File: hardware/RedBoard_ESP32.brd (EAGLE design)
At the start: 68.6 x 58.4 mm, 110 parts, among them J1 5.5x2.1mm Barrel, J13 QWIIC_RIGHT_ANGLE, J15 MICRO-SDPUSH-PUSH, J2 USB C, J3 USB_SOLDER_PADS, J5 M10NO_SILK, Q1 MBT3904DW1T1, Q11 20V/4.2A/52mΩ/1.4W, Q13 20V/4.2A/52mΩ/1.4W, Q3 20V/4.2A/52mΩ/1.4W, Q5 20V/4.2A/52mΩ/1.4W, Q7 20V/4.2A/52mΩ/1.4W, Q9 20V/4.2A/52mΩ/1.4W, U1 ESP-WROOM-3232D-NARROW, U2 CH340C, U3 LM1117, U4 3.3V, U5 MCP73831, U6 MAX17048

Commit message: Added missing Vin symbol.
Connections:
- removed net N$9: C9.+, D1.C, U3.3
- net VIN: now also C9.+, D1.C, U3.3
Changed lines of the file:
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@@
 <contactref element="J9" pad="8"/>
 <contactref element="J10" pad="8"/>
-<wire x1="45.72" y1="1.27" x2="45.72" y2="6.732" width="0" layer="19" extent="1-1"/>
+<contactref element="C9" pad="+"/>
+<contactref element="D1" pad="C"/>
+<contactref element="U3" pad="3"/>
+<wire x1="-63.64" y1="-764.54" x2="-71.3486" y2="-768.9088" width="0" layer="19" extent="1-1"/>
+<wire x1="-56.27" y1="-763.27" x2="-63.64" y2="-764.54" width="0" layer="19" extent="1-1"/>
+<wire x1="45.72" y1="1.27" x2="-56.27" y2="-763.27" width="0" layer="19" extent="1-1"/>
+<wire x1="45.72" y1="6.732" x2="45.72" y2="1.27" width="0" layer="19" extent="1-1"/>
 </signal>
 <signal name="VUSB" class="1">
@@
 <wire x1="-61.81" y1="-772.16" x2="-63.92" y2="-772.16" width="0" layer="19" extent="1-1"/>
 </signal>
-<signal name="N$9" class="1">
-<contactref element="C9" pad="+"/>
-<contactref element="D1" pad="C"/>
-<contactref element="U3" pad="3"/>
-<wire x1="-63.64" y1="-764.54" x2="-71.3486" y2="-768.9088" width="0" layer="19" extent="1-1"/>
-<wire x1="-56.27" y1="-763.27" x2="-63.64" y2="-764.54" width="0" layer="19" extent="1-1"/>
-</signal>
 <signal name="N$12">

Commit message: Changed pin name from /SS to /CS
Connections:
- net ESP32_GPIO5_!SS! renamed ESP32_GPIO5_!CS!
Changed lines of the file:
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@@
 <wire x1="0" y1="-547.37" x2="45.8" y2="15.892" width="0" layer="19" extent="1-1"/>
 </signal>
-<signal name="ESP32_GPIO5_!SS!">
+<signal name="ESP32_GPIO5_!CS!">
 <contactref element="U1" pad="29"/>
 <contactref element="J15" pad="CS/DAT3"/>

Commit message: Preliminary routed board, no labels yet.
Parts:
- LOGO1: value SFE_LOGO_NAME_FLAME6_MM -> SFE_LOGO_NAME.1_INCH; device SparkFun-Aesthetics:SFE_LOGO_NAME_FLAME_6MM -> SparkFun-Aesthetics:SFE_LOGO_NAME_.1
- moved LOGO4 973.6 mm to (10.2, 56.9), flipped to the bottom
- moved LOGO2 962.8 mm to (10.2, 51.1)
- moved R8 945.3 mm to (26.7, 38.1)
- moved D5 942.0 mm to (31.8, 38.1), turned to 180 degrees
- moved J14 939.5 mm to (19.7, 40.6), turned to 90 degrees
- moved JP10 935.5 mm to (22.2, 41.9), flipped to the bottom, turned to 90 degrees
- moved LOGO1 926.1 mm to (48.8, 12.4)
- moved LOGO3 925.7 mm to (9.91, 11.2), flipped to the bottom
- moved C17 899.9 mm to (21.6, 13.3)
- moved R25 897.9 mm to (36.8, 18.4), turned to 180 degrees
- moved Q10 895.5 mm to (33.0, 20.3), turned to 270 degrees
- moved R26 895.5 mm to (36.8, 16.5), turned to 180 degrees
- moved R24 893.5 mm to (36.8, 20.3), turned to 180 degrees
- moved R27 893.2 mm to (36.8, 14.6), turned to 180 degrees
- moved U6 891.3 mm to (17.8, 10.2)
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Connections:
- removed net SHLD: J2.SHLD1, J2.SHLD2, J2.SHLD3, J2.SHLD4
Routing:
- net ESP32_SCL: track 0.00 -> 180.8 mm, vias 0 -> 7
- net ESP32_SDA: track 0.00 -> 164.2 mm, vias 0 -> 5
- net ESP32_GPIO19_CIPO: track 0.00 -> 145.0 mm, vias 0 -> 5
- net ESP32_RXD0: track 0.00 -> 121.2 mm, vias 0 -> 5
- net ESP32_GPIO23_COPI: track 0.00 -> 114.0 mm, vias 0 -> 3
- net 5V: track 0.00 -> 114.0 mm, vias 0 -> 1
- net ESP32_GPIO18_SCK: track 0.00 -> 113.5 mm, vias 0 -> 4
- net ESP32_TXD0: track 0.00 -> 109.4 mm, vias 0 -> 6
- net V_USB: track 0.00 -> 108.9 mm, vias 0 -> 6
- net ESP32_GPIO5_!CS!: track 0.00 -> 104.5 mm, vias 0 -> 3
- net !GAUGE_ALERT!: track 0.00 -> 99.5 mm, vias 0 -> 4
- net ESP32_EN: track 0.00 -> 86.5 mm, vias 0 -> 2
- net 5V_CHG: track 0.00 -> 72.0 mm, vias 0 -> 4
- net 5V_MEAS: track 0.00 -> 64.7 mm, vias 0 -> 6
- net ESP32_GPIO4: track 0.00 -> 59.2 mm, vias 0 -> 2
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- added copper zone on layer 15, net 3.3V
- added copper zone on layer 1, net 5V_EXT
- added copper zone on layer 1, net GND
- added copper zone on layer 16, net GND
- added copper zone on layer 2, net GND
- added copper zone on layer 1, net V_BATT

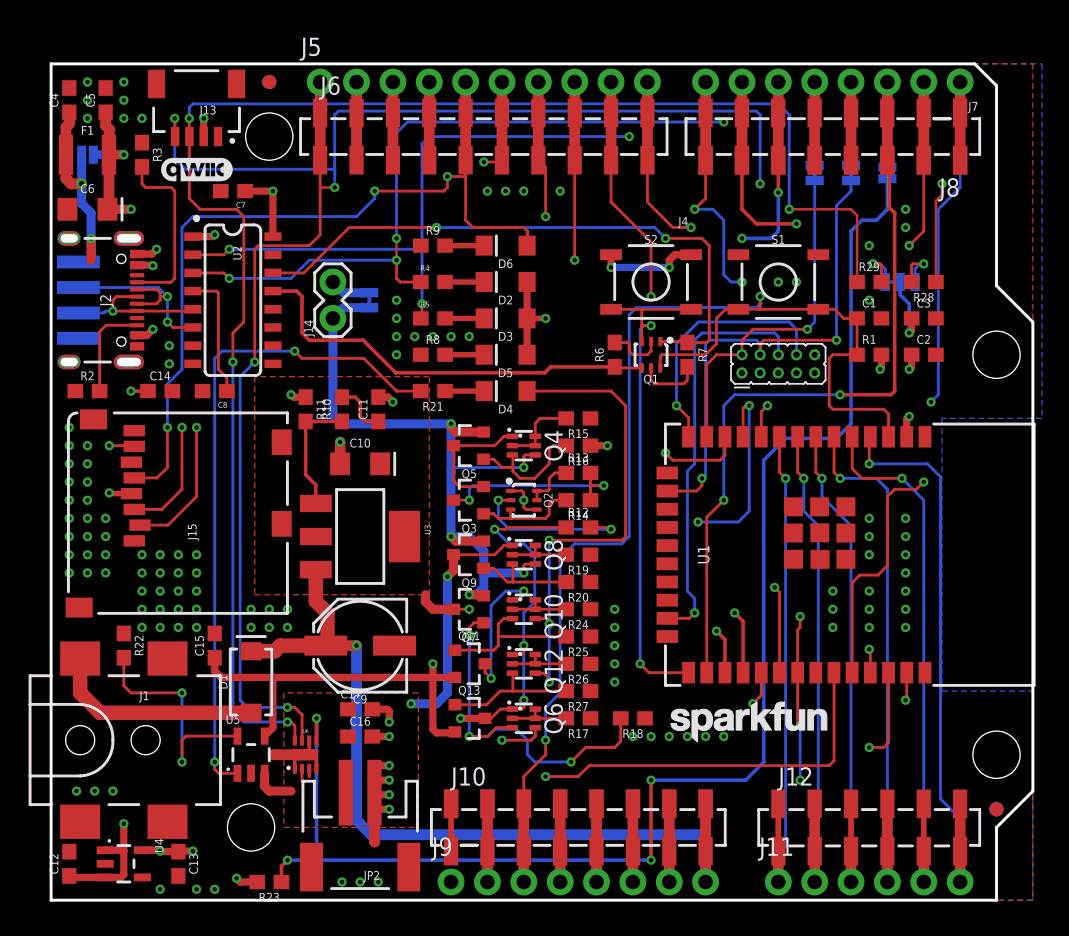
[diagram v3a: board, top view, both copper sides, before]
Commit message: Added board labels.
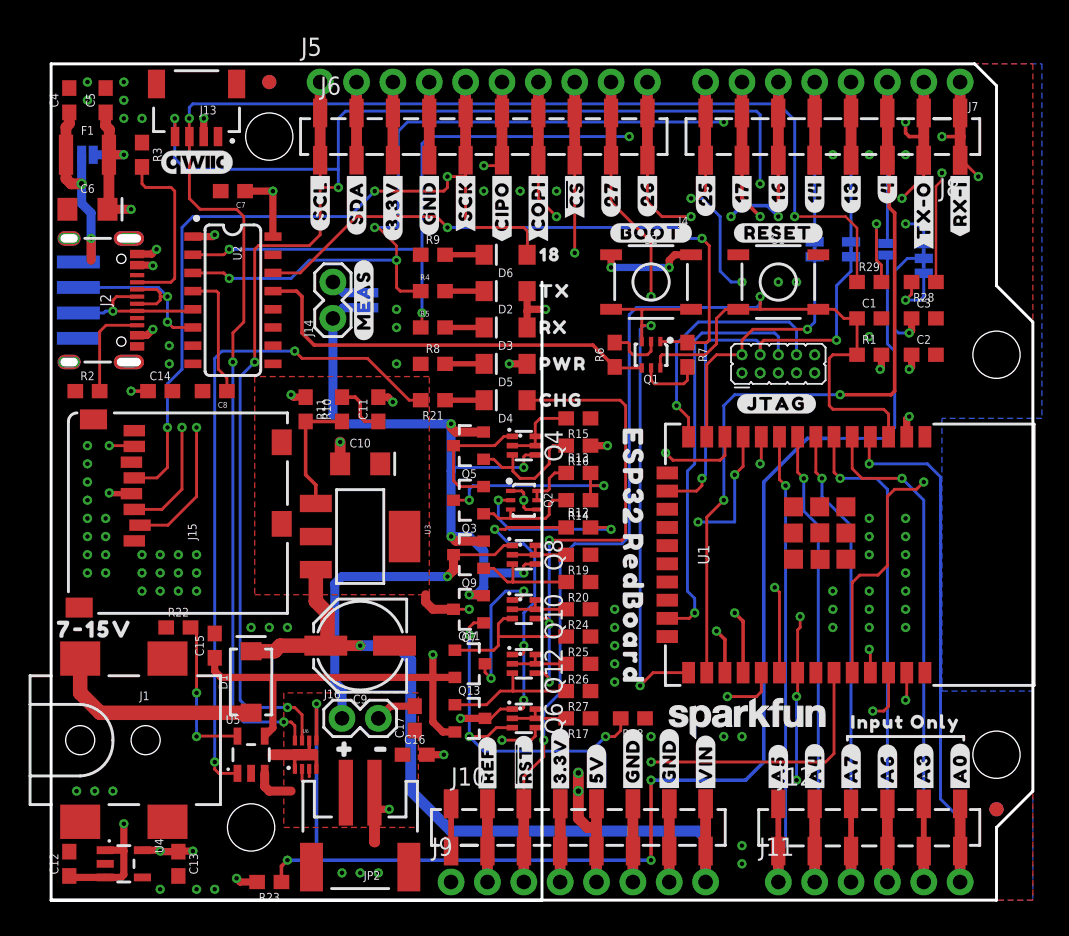
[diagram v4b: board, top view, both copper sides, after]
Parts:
- added J16: (no value), SparkFun-Connectors:1X02
- added LOGO5: SPECIAL_INSTRUCTIONS-ORDERING, SparkFun-Aesthetics:ORDERING_INSTRUCTIONS
- added LOGO6: SFE_LOGO_NAME_FLAME.2_INCH, SparkFun-Aesthetics:SFE_LOGO_NAME_FLAME_.2
- added U$10: (no value), output-ESP32:1836
- added U$11: (no value), output-ESP32:##CS##28
- added U$12: (no value), output-ESP32:#27#27
- added U$13: (no value), output-ESP32:#26#26
- added U$14: (no value), output-ESP32:TX1838
- added U$15: (no value), output-ESP32:RX1839
- added U$16: (no value), output-ESP32:PWR1837
- added U$17: (no value), output-ESP32:CHG1840
- added U$18: (no value), output-ESP32:#25#18
- added U$19: (no value), output-ESP32:#17#17
- added U$20: (no value), output-ESP32:#16#15
- added U$21: (no value), output-ESP32:#14#14
- added U$22: (no value), output-ESP32:#13#5
- added U$23: (no value), output-ESP32:#4#2
- added U$24: (no value), output-ESP32:#TX#O#0
- added U$25: (no value), output-ESP32:#RX#I#1
- added U$26: (no value), output-ESP32:#RESET#1842
- added U$27: (no value), output-ESP32:#BOOT#1841
- added U$28, U$46: (no value), output-ESP32:#JTAG#1847
- added U$29: (no value), output-ESP32:#A0#1843
- added U$3: (no value), output-ESP32:#SCL#34
- added U$30: (no value), output-ESP32:#A3#1843
- added U$31: (no value), output-ESP32:#A6#1843
- added U$32: (no value), output-ESP32:#A7#1843
- added U$33: (no value), output-ESP32:#A4#1843
- added U$34: (no value), output-ESP32:#A5#1843
- added U$35: (no value), output-ESP32:#VIN#1843
- added U$36, U$37: (no value), output-ESP32:#GND#1844
- added U$38: (no value), output-ESP32:#5V#1845
- added U$39: (no value), output-ESP32:#3#3V#1845
- added U$4: (no value), output-ESP32:#SDA#33
- added U$40: (no value), output-ESP32:##RST##1845
- added U$41: (no value), output-ESP32:#REF#1846
- added U$42, U$81: (no value), output-ESP32:#MEAS#1851
- added U$43, U$86: (no value), output-ESP32:#1849
- added U$44, U$88: (no value), output-ESP32:#1850
- added U$45: (no value), output-ESP32:#BATT#1848
- added U$47: (no value), output-ESP32:REDBOARD321856
- added U$48: (no value), output-ESP32:ESP321855
- added U$49: (no value), output-ESP32:7#15V32321861
- added U$5: (no value), output-ESP32:#3#3V#33
- added U$50: (no value), output-ESP32:#39#A3#32321865
- added U$51: (no value), output-ESP32:#36#A0#32321865
- added U$52: (no value), output-ESP32:#34#A6#32321865
- added U$53: (no value), output-ESP32:#35#A7#32321865
- added U$54: (no value), output-ESP32:#32#A4#32321865
- added U$55: (no value), output-ESP32:#33#A5#32321865
- added U$56: (no value), output-ESP32:#VIN#32321865
- added U$57, U$60: (no value), output-ESP32:#GND#32321866
- added U$58: (no value), output-ESP32:#5V#32321867
- added U$59: (no value), output-ESP32:#3#3V#32321867
- added U$6: (no value), output-ESP32:#GND#32
- added U$61: (no value), output-ESP32:##RST##32321867
- added U$62: (no value), output-ESP32:#IOREF#32321868
- added U$63: (no value), output-ESP32:#3#RX#I#32321869
- added U$64: (no value), output-ESP32:#1#TX#O#32321869
- added U$65: (no value), output-ESP32:#4#32321869
- added U$66: (no value), output-ESP32:#13#TCK#32321869
- added U$67: (no value), output-ESP32:#14#TMS#32321869
- added U$68: (no value), output-ESP32:#16#32321869
- added U$69: (no value), output-ESP32:#17#32321869
- added U$7: (no value), output-ESP32:#SCK#31
- added U$70: (no value), output-ESP32:#25#32321869
- added U$71: (no value), output-ESP32:#26#32321869
- added U$72: (no value), output-ESP32:#5##CS##32321869
- added U$73: (no value), output-ESP32:#23#COPI#32321869
- added U$74: (no value), output-ESP32:#19#CIPO#32321869
- added U$75: (no value), output-ESP32:#18#SCK#32321869
- added U$76: (no value), output-ESP32:#21#SDA#32321869
- added U$77: (no value), output-ESP32:#22#SCL#32321869
- added U$78: (no value), output-ESP32:#27#32321869
- added U$79: (no value), output-ESP32:#GND#32321869
- added U$8: (no value), output-ESP32:#CIPO#30
- added U$80: (no value), output-ESP32:#3#3V#32321869
- added U$82: (no value), output-ESP32:#BYP#35
- added U$83: (no value), output-ESP32:D#32321863
- added U$84: (no value), output-ESP32:D#32321862
- added U$85: (no value), output-ESP32:G32321864
- added U$89: (no value), output-ESP32:#I2C#1855
- added U$9: (no value), output-ESP32:#COPI#29
- added U$90: (no value), output-ESP32:##ALERT##1852
- added U$91: (no value), output-ESP32:#TMS#1854
- added U$92: (no value), output-ESP32:#TCK#1853
- added U$93: (no value), output-ESP32:ESP32_REDBOARD321857
- added U$94: (no value), output-ESP32:MADE_IN_THE_USA321857
- added U$96, U$97: (no value), output-ESP32:INPUT_ONLY321867
- moved FRAME1 79.2 mm to (5.59, 60.7)
- moved LOGO3 11.9 mm to (2.29, 2.03)
- moved JP12 5.33 mm to (58.4, 45.5)
- moved JP13 5.33 mm to (55.9, 45.5)
- moved JP14 5.33 mm to (53.3, 45.5)
- moved R22 4.02 mm to (8.89, 19.1), turned to 0 degrees
- moved C16 4.02 mm to (25.4, 10.2)
- moved C17 3.86 mm to (25.4, 12.7), turned to 90 degrees
- moved JP11 2.33 mm to (61.0, 44.8), turned to 270 degrees
- moved D4 0.64 mm to (31.8, 34.9)
- moved R21 0.64 mm to (26.7, 34.9)
- moved D2 0.63 mm to (31.8, 42.5)
- moved D3 0.63 mm to (31.8, 40.0)
- moved D5 0.63 mm to (31.8, 37.5)
- moved D6 0.63 mm to (31.8, 45.1)
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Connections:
- net GND: now also J16.2
- net V_BATT: now also J16.1
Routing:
- net V_BATT: track 21.3 -> 28.0 mm, vias 2 -> 1
- net ESP32_RXD0: track 121.2 -> 115.3 mm, vias 5 -> 6
- net N$14: track 16.6 -> 10.7 mm
- net ESP32_GPIO17: track 49.6 -> 44.0 mm
- net ESP32_GPIO4: track 59.2 -> 64.6 mm
- net ESP32_GPIO14_HDR: track 11.3 -> 16.6 mm
- net ESP32_GPIO13_HDR: track 11.3 -> 16.6 mm
- net ESP32_GPIO13_TCK: track 35.2 -> 29.8 mm
- net ESP32_GPIO14_TMS: track 24.3 -> 19.0 mm
- net N$20: track 3.74 -> 8.60 mm, vias 1 -> 2
- net ESP32_GPIO26: track 46.7 -> 42.6 mm
- net 5V: track 114.0 -> 110.6 mm, vias 1 -> 3
- net 3.3V: track 45.6 -> 48.1 mm, vias 12 -> 13
- net !GAUGE_ALERT!: track 99.5 -> 97.4 mm
- net ESP32_GPIO25: track 31.2 -> 33.3 mm
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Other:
- outline, holes or cut-outs redrawn
- board text added: "- Finish: HASL-Lead Free"

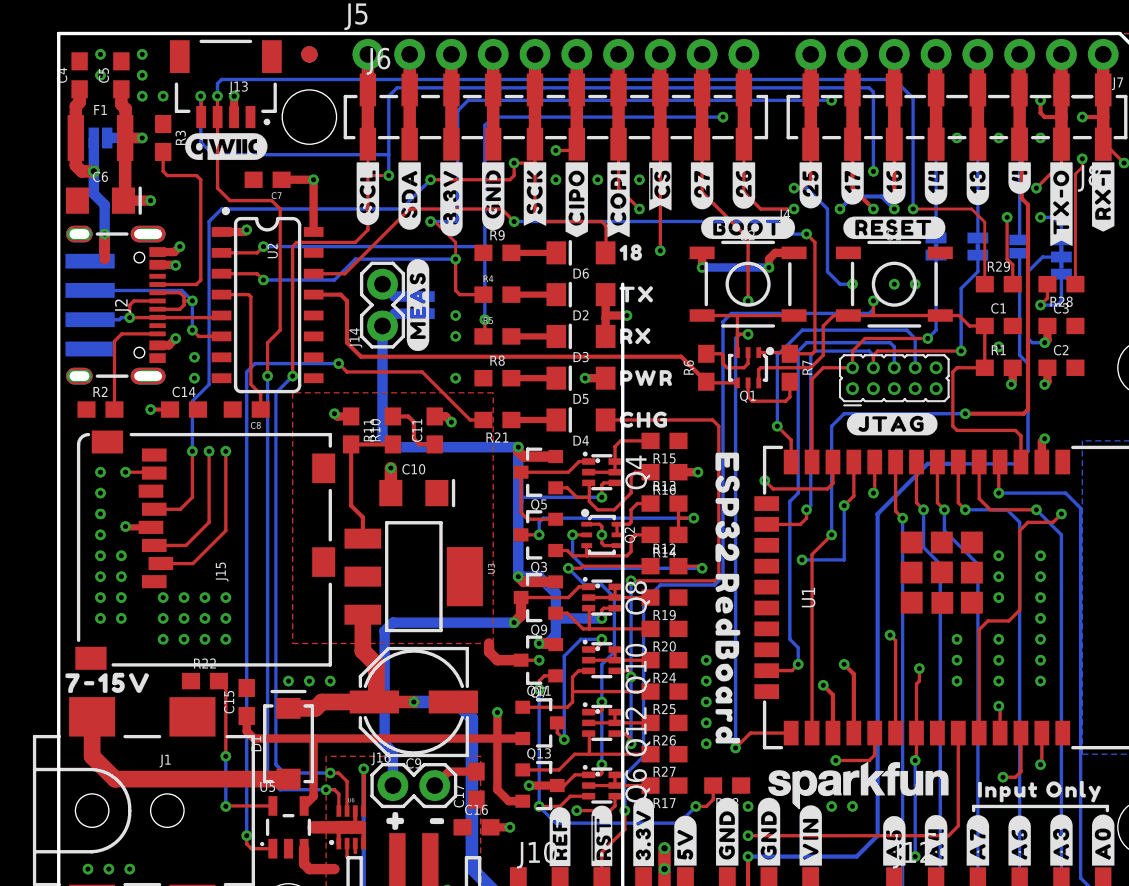
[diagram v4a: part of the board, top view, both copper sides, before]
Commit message: Added ordering instructions; added production files.
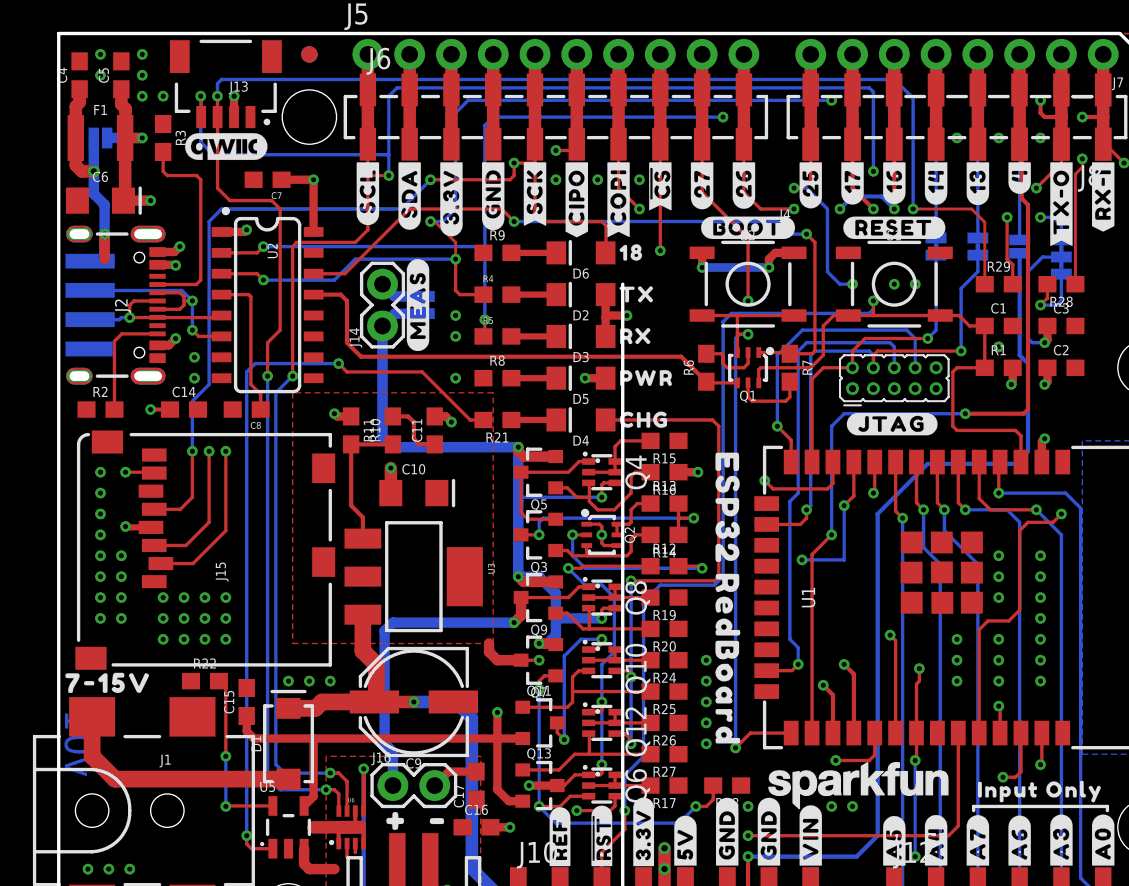
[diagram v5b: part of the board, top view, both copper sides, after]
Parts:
- U$65: device output-ESP32:#4#32321869 -> output-ESP32:##ALERT##4#321866
- moved U$65 0.13 mm to (58.4, 56.5)
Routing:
- net ESP32_TXD0: track 110.9 -> 110.2 mm
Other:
- board text added: "- 4 Layer Board"
- board text added: "- Board thickness is 1.6mm"
- board text added: "- No clean process"
- board text added: "v01"
- board text removed: "Units in inches"

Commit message: Changed board per Nathan's recommendations; added production files.
- Changed SPI pins nomenclatures.
- Fixed silkscreens.
- Replaced SD card socket with an updated one.
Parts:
- J14, J16: device SparkFun-Connectors:1X02 -> SparkFun-Connectors:1X02_NO_SILK
- J15: value MICRO-SDPUSH-PUSH -> MICRO-SD-PUSH-PUSH-EXT-PIN; device SparkFun-Connectors:MICRO-SD-SOCKET -> SparkFun-Connectors:MICROSD-EXTERNALPIN
- U$50: device output-ESP32:#39#A3#32321865 -> output-ESP32:#39#A3#321862
- U$51: device output-ESP32:#36#A0#32321865 -> output-ESP32:#36#A0#321862
- U$53: device output-ESP32:#35#A7#32321865 -> output-ESP32:#35#A7#321862
- U$55: device output-ESP32:#33#A5#32321865 -> output-ESP32:#34#A6#321862
- U$56: device output-ESP32:#VIN#32321865 -> output-ESP32:#VIN#321862
- U$57, U$60: device output-ESP32:#GND#32321866 -> output-ESP32:#GND#321863
- U$58: device output-ESP32:#5V#32321867 -> output-ESP32:#5V#321864
- U$59: device output-ESP32:#3#3V#32321867 -> output-ESP32:#3#3V#321864
- U$61: device output-ESP32:##RST##32321867 -> output-ESP32:##RESET##321864
- U$62: device output-ESP32:#IOREF#32321868 -> output-ESP32:#IOREF#321865
- U$73: device output-ESP32:#23#COPI#32321869 -> output-ESP32:#23#PICO#321866
- U$74: device output-ESP32:#19#CIPO#32321869 -> output-ESP32:#19#POCI#321866
- U$79: device output-ESP32:#GND#32321869 -> output-ESP32:#GND#321866
- U$8: device output-ESP32:#CIPO#30 -> output-ESP32:#POCI#30
- U$80: device output-ESP32:#3#3V#32321869 -> output-ESP32:#3#3V#321866
- U$9: device output-ESP32:#COPI#29 -> output-ESP32:#PICO#29
- moved LOGO1 36.8 mm to (15.4, 28.4), turned to 270 degrees
- moved R23 33.2 mm to (48.3, 5.08), turned to 270 degrees
- moved R22 18.9 mm to (15.2, 1.27), turned to 180 degrees
- moved C14 16.4 mm to (17.1, 48.9), turned to 90 degrees
- moved J15 16.0 mm to (2.03, 27.3), turned to 270 degrees
- moved C8 14.3 mm to (6.35, 48.9), turned to 90 degrees
- moved U$49 4.83 mm to (7.87, 19.1)
- moved R3 3.70 mm to (8.26, 48.9)
- moved R2 3.24 mm to (5.71, 36.2), turned to 180 degrees
- turned C11 to 270 degrees
- turned U$81 to 90 degrees
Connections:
- removed net ESP32_GPIO19_CIPO: J15.DO/DAT0, J5.6, J6.6A, J6.6B, U1.31
- removed net ESP32_GPIO23_COPI: J15.DI/CMD, J5.7, J6.7A, J6.7B, U1.37
- new net ESP32_GPIO19_POCI: J15.7, J5.6, J6.6A, J6.6B, U1.31
- new net ESP32_GPIO23_PICO: J15.3, J5.7, J6.7A, J6.7B, U1.37
- net 3.3V: now also J15.4; no longer J15.VCC
- net ESP32_GPIO18_SCK: now also J15.5; no longer J15.SCLK
- net ESP32_GPIO5_!CS!: now also J15.2; no longer J15.CS/DAT3
- net GND: now also J15.10, J15.11, J15.12, J15.13, J15.6; no longer J15.GND, J15.GND1, J15.GND3
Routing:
- net ESP32_GPIO19_POCI: track 0.00 -> 149.6 mm, vias 0 -> 5
- net ESP32_GPIO19_CIPO: track 143.9 -> 0.00 mm, vias 5 -> 0
- net ESP32_GPIO23_PICO: track 0.00 -> 114.5 mm, vias 0 -> 3
- net ESP32_GPIO23_COPI: track 114.3 -> 0.00 mm, vias 3 -> 0
- net V_USB: track 108.9 -> 115.9 mm, vias 6 -> 5
- net CC1: track 12.5 -> 6.75 mm
- net N$6: track 8.94 -> 14.4 mm, vias 0 -> 2
- net N$14: track 10.7 -> 15.0 mm, vias 2 -> 0
- net GND: track 49.2 -> 53.0 mm, vias 93 -> 83
- net ESP32_GPIO18_SCK: track 113.5 -> 115.9 mm
- net 3.3V: track 48.1 -> 50.4 mm, vias 13 -> 12
- net !GAUGE_ALERT!: track 97.4 -> 95.3 mm
- net 5V_EXT: track 39.5 -> 38.2 mm
- net ESP32_GPIO5_!CS!: track 103.7 -> 104.7 mm
- net ESP32_GPIO12_TDI: track 17.8 -> 18.9 mm
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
